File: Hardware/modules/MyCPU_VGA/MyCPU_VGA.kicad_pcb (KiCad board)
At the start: 4 copper layers, 83.3 x 68.2 mm, 23 parts, among them J1 Bus_PCI_6502, J2 MyCPU Bus, U1 74HC138, U2 74HC138, U3 74AHC541, U4 74HCT574, U5 74HCT574, U6 74HCT574, U7 74HC00, U8 74HC02

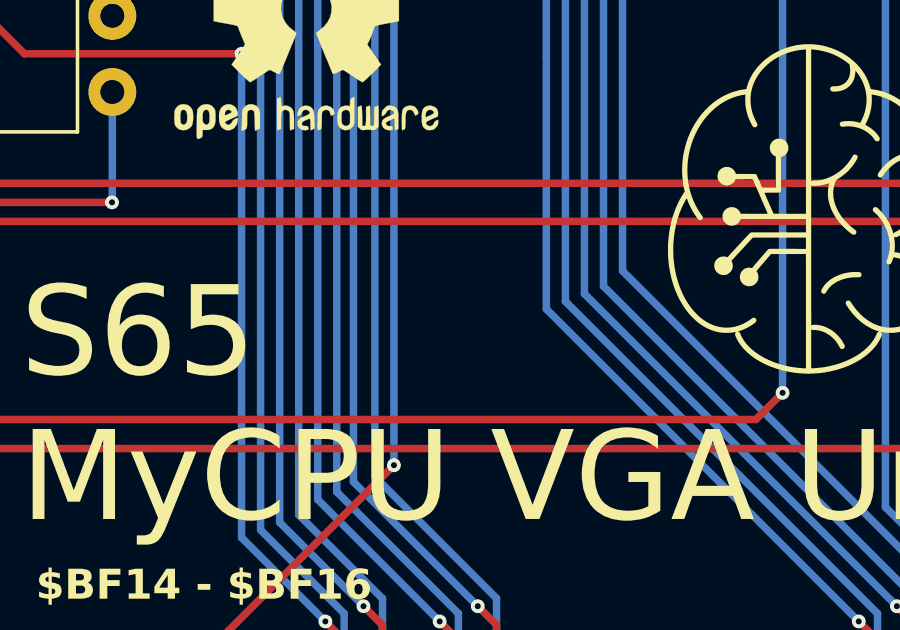
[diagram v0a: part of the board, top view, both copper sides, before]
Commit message: Hardware Review Pt. 1 fix Address Decoding for Strobe Generators add bulk capacitance to every board fix wiring of Prototyping Board
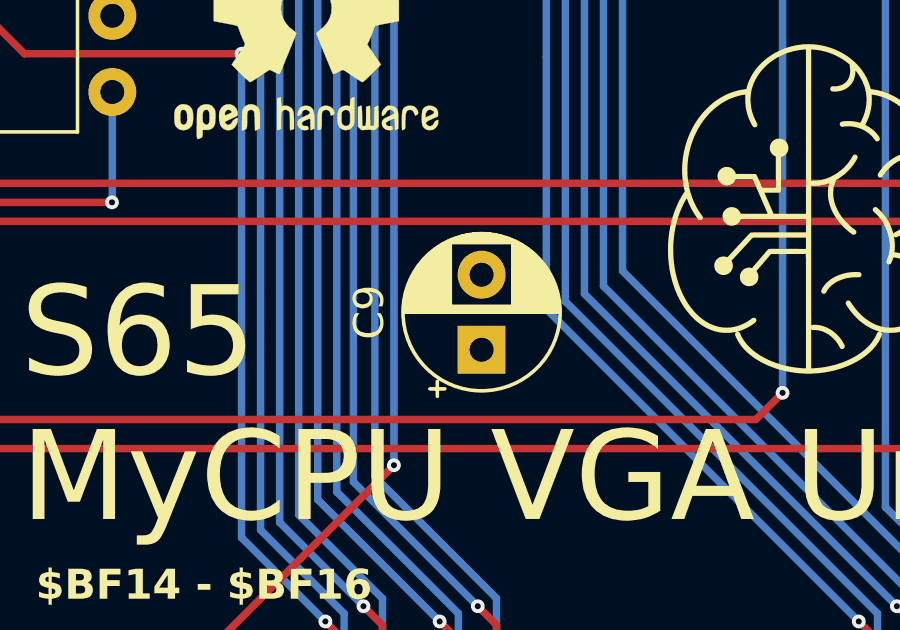
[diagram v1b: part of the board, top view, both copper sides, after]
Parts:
- added C9: 10µ, Capacitor_THT:CP_Radial_D5.0mm_P2.50mm, F.Cu at (173.1, 109.4)
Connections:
- J1 pad A11: /A13 -> unconnected-(J1-A13-PadA11)
- J1 pad A12: /A15 -> unconnected-(J1-A15-PadA12)
- J1 pad A25: /~{ROM} -> unconnected-(J1-~{ROM}-PadA25)_0
- J1 pad A27: /~{IRQ_0.0} -> unconnected-(J1-~{IRQ_0.0}-PadA27)_0
- J1 pad A28: /~{IRQ_0.1} -> unconnected-(J1-~{IRQ_0.1}-PadA28)
- J1 pad A29: /~{IRQ_0.2} -> unconnected-(J1-~{IRQ_0.2}-PadA29)_0
- J1 pad A30: /~{IRQ_0.3} -> unconnected-(J1-~{IRQ_0.3}-PadA30)_0
- J1 pad A31: /~{IRQ_0.4} -> unconnected-(J1-~{IRQ_0.4}-PadA31)_0
- J1 pad A32: /~{IRQ_0.5} -> unconnected-(J1-~{IRQ_0.5}-PadA32)
- J1 pad A33: /~{IRQ_0.6} -> unconnected-(J1-~{IRQ_0.6}-PadA33)
- J1 pad A34: /~{IRQ_0.7} -> unconnected-(J1-~{IRQ_0.7}-PadA34)_0
- J1 pad A38: /SYNC_VPA -> unconnected-(J1-Sync/VPA-PadA38)
- J1 pad A39: /Ø2/VDA -> unconnected-(J1-Ø2/VDA-PadA39)_0
- J1 pad A41: /~{RDY} -> unconnected-(J1-~{RDY}-PadA41)
- J1 pad A42: /~{BE} -> unconnected-(J1-~{BE}-PadA42)
- J1 pad A45: /E -> unconnected-(J1-E-PadA45)_0
- J1 pad A53: /RAM_0 -> unconnected-(J1-RAM0-PadA53)
- J1 pad A54: /RAM_1 -> unconnected-(J1-RAM1-PadA54)_0
- J1 pad A55: /RAM_2 -> unconnected-(J1-RAM2-PadA55)
- J1 pad A56: /RAM_3 -> unconnected-(J1-RAM3-PadA56)_0
- J1 pad A58: /RAM_4 -> unconnected-(J1-RAM4-PadA58)
- J1 pad A59: /RAM_5 -> unconnected-(J1-RAM5-PadA59)_0
- J1 pad A60: /RAM_6 -> unconnected-(J1-RAM6-PadA60)_0
- J1 pad A61: /RAM_7 -> unconnected-(J1-RAM7-PadA61)
- J1 pad A8: /A9 -> unconnected-(J1-A9-PadA8)_0
- J1 pad A9: /A11 -> unconnected-(J1-A11-PadA9)
- J1 pad B11: /A12 -> unconnected-(J1-A12-PadB11)
- J1 pad B12: /A14 -> unconnected-(J1-A14-PadB12)_0
- J1 pad B24: /~{L_RAM} -> unconnected-(J1-~{L_RAM}-PadB24)
- J1 pad B25: /~{H_RAM} -> unconnected-(J1-~{H_RAM}-PadB25)
- J1 pad B27: /~{IRQ} -> unconnected-(J1-~{IRQ}-PadB27)_0
- J1 pad B28: /~{IRQ_0} -> unconnected-(J1-~{IRQ_0}-PadB28)_0
- J1 pad B29: /~{IRQ_1} -> unconnected-(J1-~{IRQ_1}-PadB29)
- J1 pad B30: /~{IRQ_2} -> unconnected-(J1-~{IRQ_2}-PadB30)
- J1 pad B31: /~{IRQ_3} -> unconnected-(J1-~{IRQ_3}-PadB31)_0
- J1 pad B32: /~{IRQ_4} -> unconnected-(J1-~{IRQ_4}-PadB32)
- J1 pad B33: /~{NMI} -> unconnected-(J1-~{NMI}-PadB33)
- J1 pad B34: /PAGE -> unconnected-(J1-PAGE_ROM-PadB34)
- J1 pad B38: /~{VP} -> unconnected-(J1-~{VP}-PadB38)
- J1 pad B39: /~{ML} -> unconnected-(J1-~{ML}-PadB39)
- J1 pad B46: /M/X -> unconnected-(J1-M/~{X}-PadB46)
- J1 pad B53: /ROM_0 -> unconnected-(J1-ROM0-PadB53)
- J1 pad B54: /ROM_1 -> unconnected-(J1-ROM1-PadB54)_0
- J1 pad B55: /ROM_2 -> unconnected-(J1-ROM2-PadB55)_0
- J1 pad B56: /ROM_3 -> unconnected-(J1-ROM3-PadB56)
- J1 pad B58: /ROM_4 -> unconnected-(J1-ROM4-PadB58)_0
- J1 pad B59: /ROM_5 -> unconnected-(J1-ROM5-PadB59)
- J1 pad B60: /ROM_6 -> unconnected-(J1-ROM6-PadB60)
- J1 pad B61: /ROM_7 -> unconnected-(J1-ROM7-PadB61)_0
- J1 pad B8: /A8 -> unconnected-(J1-A8-PadB8)
- J1 pad B9: /A10 -> unconnected-(J1-A10-PadB9)
- U2 pad 7: /~{CONTROL} -> unconnected-(U2-~{Y7}-Pad7)

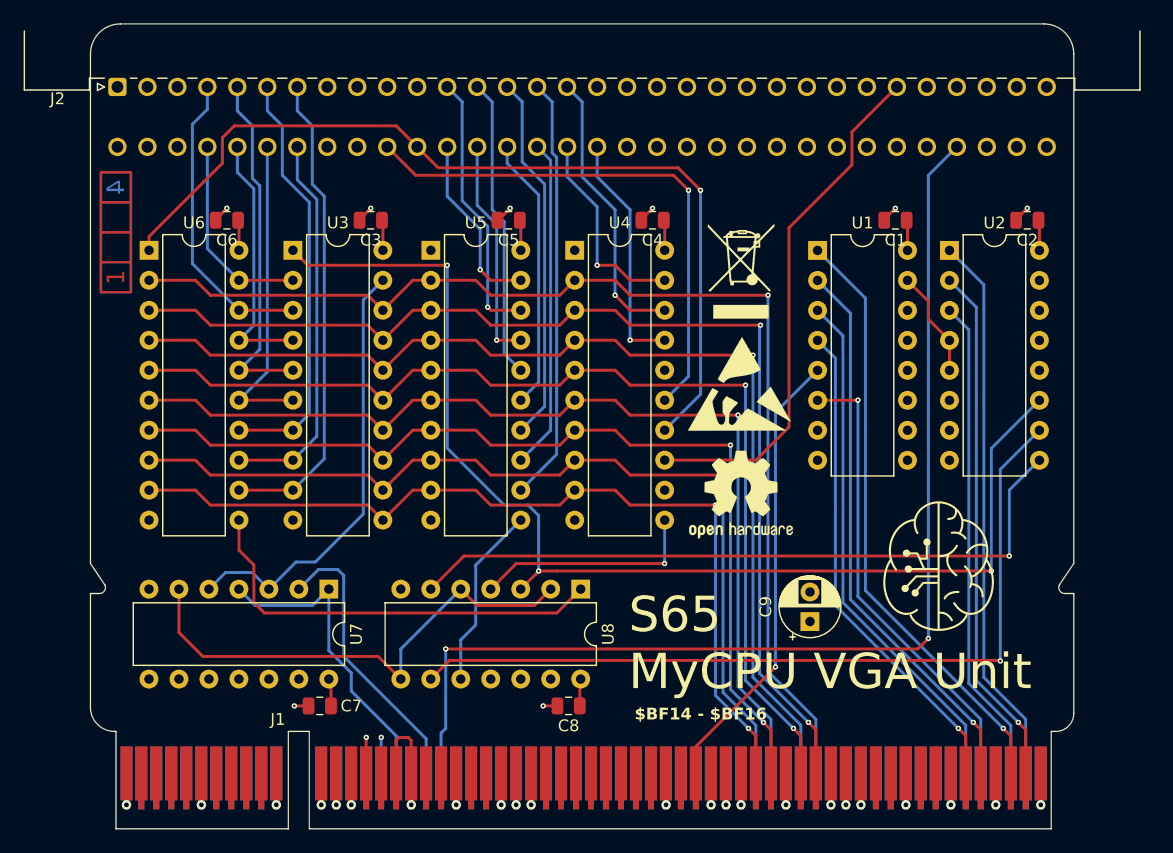
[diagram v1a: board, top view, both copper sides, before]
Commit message: Big Review Update - Changed Copper Pours on all PCBs - Implemented errors found at review - fixed some additional errors
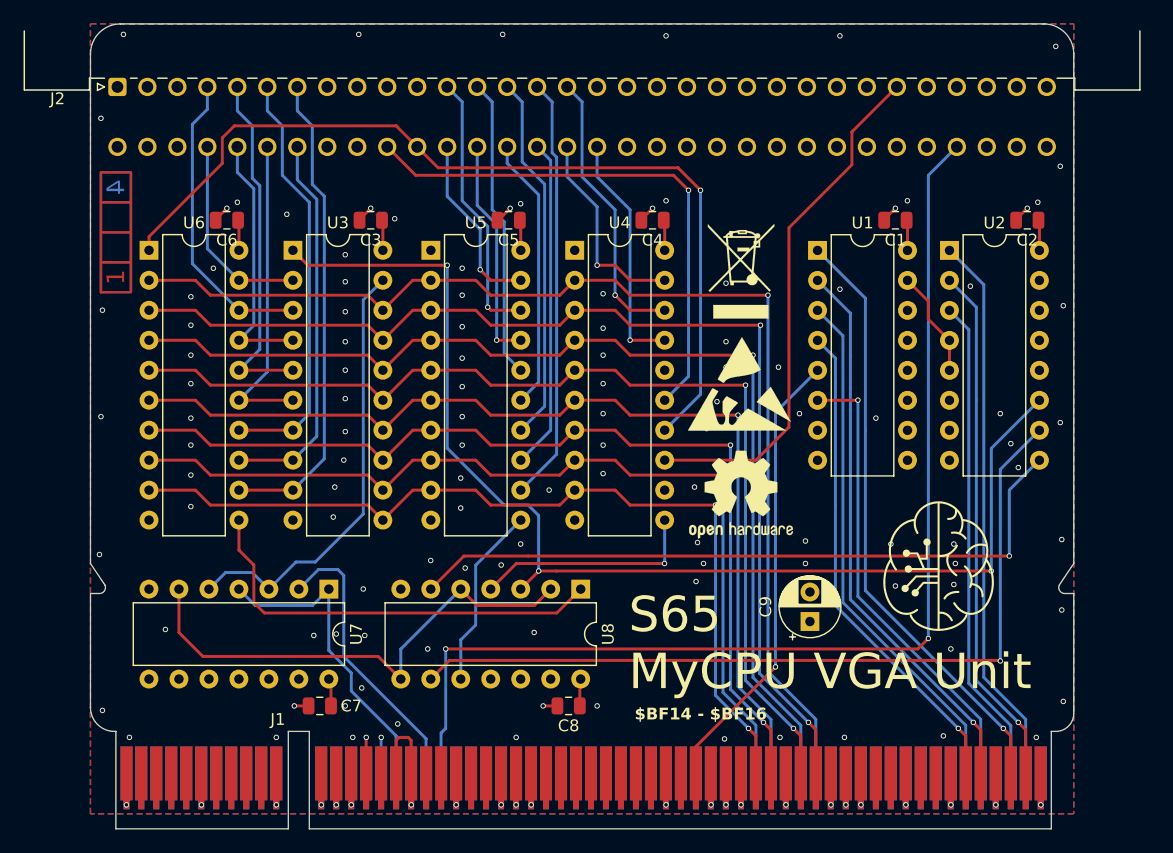
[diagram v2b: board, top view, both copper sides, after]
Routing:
- net +5V: vias 4 -> 114
- added copper zone on B.Cu, net +5V
- added copper zone on F.Cu, net +5V
- added copper zone on In1.Cu, net GND
- removed copper zone on In1.Cu, net +5V
